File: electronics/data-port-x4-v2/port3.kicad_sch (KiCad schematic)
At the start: 30 parts, among them J301 PORT3, J302 PINS3, U301 TPS2553DBVR-1, U302 INA226AIDGSR, U303 USBLC6-2SC6, U305 H5VU25UC, U306 H5VU25UC, U307 LSF0108RKSR

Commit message: DATA x4 v2: datasheet audit fixes 1-9, conservative options, CFG_SEL 110
The DATA x4 v2 datasheet audit's fixes, approved by the user, plus the
conservative options that close U2, U8, U9 and U10:

- Core regulator (fixes 1-3).
  - L1 on a polarity-marked land: bench:L_Abracon_AOTA-B201610, RP's
    0.7 x 1.7 mm pads, the dot on pad 1 = +1V1 (U1's answer).
  - The block is Raspberry Pi's RP2350B Minimal R4-S1 one, turned 180
    degrees with U11, at their coordinates.  CIN and COUT sit on RP's
    0402 land (bench:C_0402_1005Metric_RP), so LX runs 0.3 mm between
    them.
  - Copper: their F.Cu areas (LX, +1V1 with the two V_OUT vias, PGND
    with its two vias, VIN) and their settings; VREG_FB taken at the
    V_OUT vias; CFILT on its own via.
  - The F.Cu GND pour leaves a hole round the block, so PGND meets the
    main GND only through its two vias.  No copper under LX and L1 on
    In1, In2 and B.Cu.
- Fix 4: C47 (DVDD pin 32) 100 nF -> 4.7 uF.
- Fix 5: R40 47k -> 10k, so GPIO45 stays >= -0.48 V; formula updated.
- Fix 6: UMW MAX809S (U5, C347371) drives the hub's RESET_N in place of
  R2/C6; C6 is its 100 nF.
- Fix 7: two H5VU25UC per port in flow-through.  VREF and RESET/BOOT
  sit at the header's two ends, so one part per end:
  - U108-U408 take VREF (logic only);
  - U109-U409 take RESET_N/BOOT_N with the 1k right behind them, fitted
    on the base too (schematic review N4).
  VREF and ports 1-3's RESET_N are drawn into their ESD pins; all 12
  lines checked in flow-through.
- Fixes 8, 9: the VREF isolation wording and the firmware rule (switches
  open below 0.65 V, in multi-dut-node.md); +5V_MX ~1-4 mA, FB1 and U3
  stale lines gone.
- Conservative options:
  - U2: R10 1M across XI-XO (C26083);
  - U8: R115-R415 100k in series with GPIO40-43;
  - U9: R11, R12 10k on the TCA6408A RESETs;
  - U10: C7, C8 4.7 uF.
- Hub on CFG_SEL 110, internal defaults with straps disabled (U11, U12
  answered by the user).  CFG_SEL1 and CFG_SEL2 pull up through their
  RN2/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
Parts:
- added R315: 100k, Resistor_SMD:R_0402_1005Metric, symbol Device:R
- added U308, U309: H5VU25UC, bench:DFN2510-10L_2.5x1.0mm_P0.5mm, symbol Power_Protection:TPD4E05U06DQA
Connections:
- net CP_VREF3: now also R315.1
- net GND: now also U308.3 (GND), U308.8 (GND), U309.3 (GND), U309.8 (GND)
- net PORT3_BOOT_N: now also U309.2 (D1-), U309.9 (NC)
- net PORT3_RST_N: now also U309.5 (D2-), U309.6 (NC)
- net PORT3_VREF: now also U308.5 (D2-), U308.6 (NC)
- new net CP_ADC3: R315.2
- no-connect marks 2 -> 12
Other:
- note added: "ESD on the header's VREF (U308, in flow-through: header → ESD → LSF0108 and divider) and on RESET_N / BOOT_N (U309: header → ESD → 1k)"

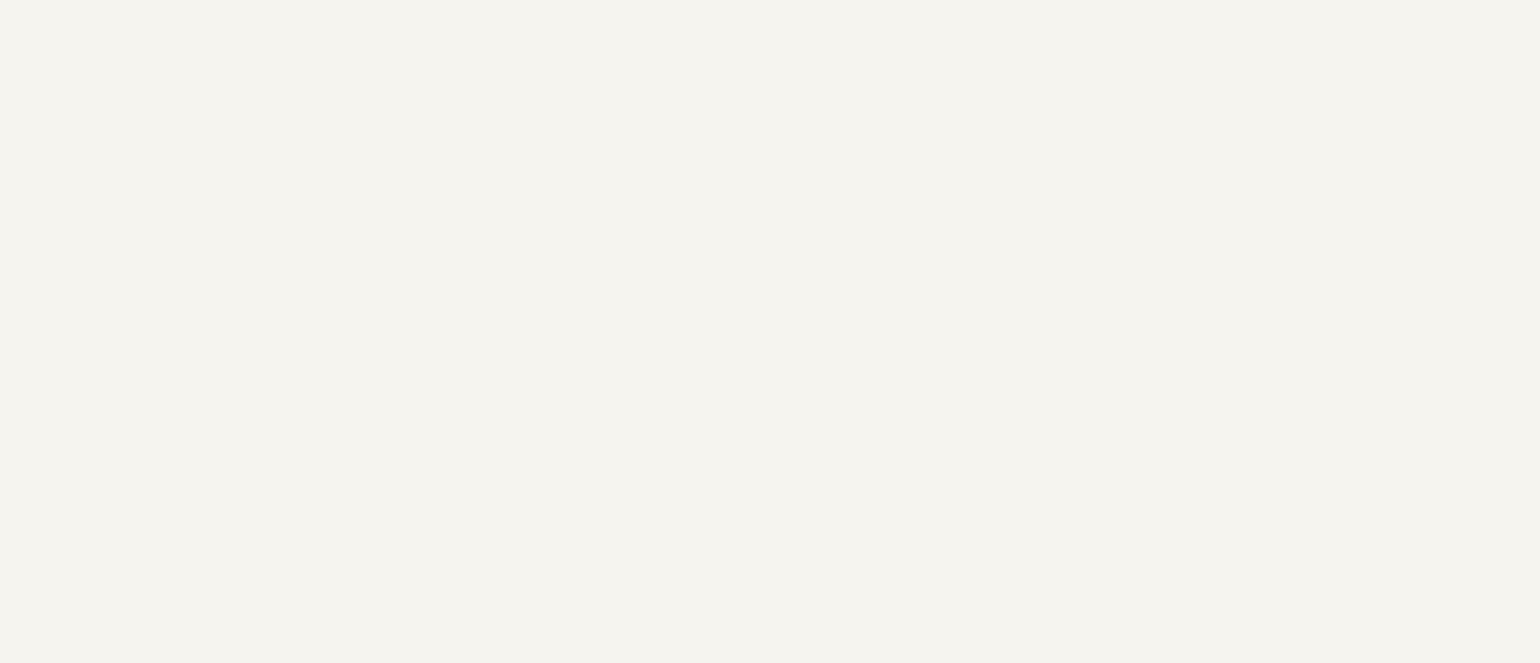
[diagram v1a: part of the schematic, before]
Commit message: DATA x4 v2: 32 labelled bring-up test points on the rear face
Eve's DFT rule on the DATA x4 v2.  Bare pads on B.Cu, mask open, no
paste, out of the BOM and the CPL (no part, no fee).  Each is named on
B.SilkS.  Supplies and GND are 1.5 mm, signals 1.0 mm (main's
"testpad1").  One table in design.py (TPS) holds every position, and
each sheet places its own.

- Co-processor row along the top edge: BOOT, RUN, SWDIO, SWCLK, GND,
  +3V3_CP.  SWD moves here from the front face.  +1V1 sits under the
  chip, on its own rear track.
- Matrix, left column: DAT, CK, STB2, GND, -5V, +5V_MX, GND; STB1 and
  MX RST on their own rear tracks.
- Supplies by the LDO: +3V3, GND, the lead's +5V.
- Hub: HUB RST, GND, 1V8.  Below J1: INT, SDA, SCL (the board side of
  the lead's isolation) and GND.
- Each port's FAULT_N (TP101-TP401) on its own rear track, and a GND by
  each pair's expander.
- Left out: VREF, RESET_N and BOOT_N (on the headers), the lead's lines
  (on J1) and the USB pairs.
- The logic's pads are marked LOGIC ONLY: the base leaves those parts
  off, so they float there.

Every pad is more than 2 mm from the THT pads and from J1, and clear of
the cradle ends, the push band and the notches.  The closest are TP23,
2.0 mm from J1's courtyard, and TP27, 2.1 mm from J101.

Routing: the old routing is seeded as protected wiring, so Freerouting
only adds the new links.  Where it gave up, the pad sits on a rear track
of its own net, or a short drawn link joins it (RUN onto CP_RUN's track,
+3V3_CP through a via to FB2).  The import's tidy pass is applied.

Checks: ERC 0, DRC 0 errors, unconnected 0, parity 0.  The 4
silk_over_copper warnings are the same on main.  Flow-through ESD check
BAD 0.  The fab outputs, panel, renders and GLBs are regenerated; the
BOM and CPL are unchanged.  docs/electronics.md lists the points, and
the "Test pads" table gains the board.

Co-Authored-By: Claude Opus 5.5 <noreply@anthropic.com>
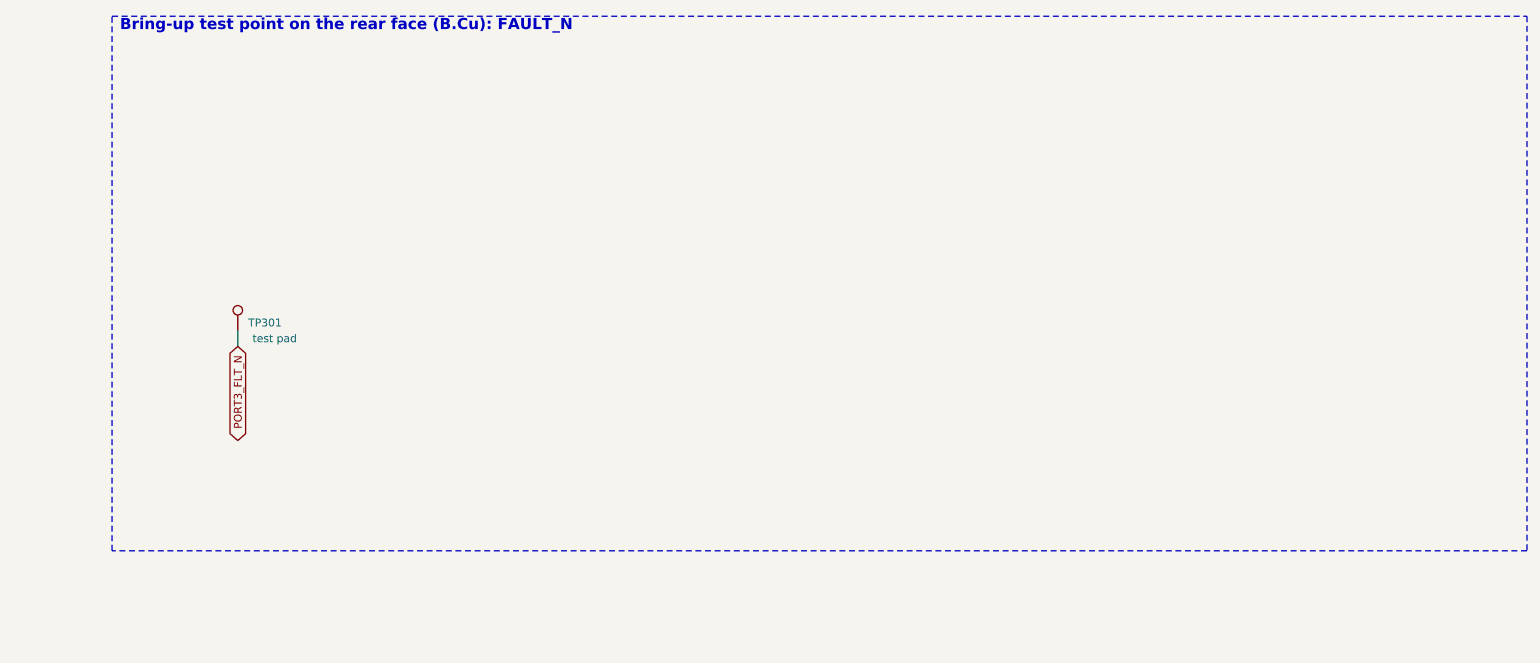
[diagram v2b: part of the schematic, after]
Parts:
- added TP301: test pad, TestPoint:TestPoint_Pad_D1.0mm, symbol Connector:TestPoint
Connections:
- net PORT3_FLT_N: now also TP301.1
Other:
- note added: "Bring-up test point on the rear face (B.Cu): FAULT_N"
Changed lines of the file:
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@@
 	)
 	(symbol
+		(lib_id "Connector:TestPoint")
+		(at 629.92 76.2 0)
+		(unit 1)
+		(exclude_from_sim no)
+		(in_bom no)
+		(on_board yes)
+		(dnp no)
+		(fields_autoplaced yes)
+		(property "Reference" "TP301"
+			(at 634.307 74.93 0)
+			(effects
+				(font
+					(size 1.27 1.27)
+				)
+			)
+		)
+		(property "Value" "test pad"
+			(at 635.882 77.47 0)
+			(effects
+				(font
+					(size 1.27 1.27)
+				)
+			)
+		)
+		(property "Footprint" "TestPoint:TestPoint_Pad_D1.0mm"
+			(at 629.92 76.2 0)
+			(effects
+				(font
+					(size 1.27 1.27)
+				)
+				(hide yes)
+			)
+		)
+		(property "Datasheet" ""
+			(at 629.92 76.2 0)
+			(effects
+				(font
+					(size 1.27 1.27)
+				)
+				(hide yes)
+			)
+		)
+		(property "Description" ""
+			(at 629.92 76.2 0)
+			(effects
+				(font
+					(size 1.27 1.27)
+				)
+				(hide yes)
+			)
+		)
+		(property "MPN" "test pad"
+			(at 629.92 76.2 0)
+			(effects
+				(font
+					(size 1.27 1.27)
+				)
+				(hide yes)
+			)
+		)
+		(property "Manufacturer" "-"
+			(at 629.92 76.2 0)
+			(effects
+				(font
+					(size 1.27 1.27)
+				)
+				(hide yes)
+			)
+		)
+		(pin "1"
+		)
+		(instances
+			(project "data-port-x4-v2"
+				(path "/6eede3c9-04e8-5df8-9dbf-dd766ca3200a/76303e69-a9f7-592c-9301-ccf39b66bdac"
+					(reference "TP301")
+					(unit 1)
+				)
+			)
+		)
+	)
+	(wire
+		(pts
+			(xy 629.92 76.2)
+			(xy 629.92 78.74)
+		)
+		(stroke
+			(width 0)
+			(type default)
+		)
+	)
+	(global_label "PORT3_FLT_N"
+		(shape bidirectional)
+		(at 629.92 78.74 270)
+		(fields_autoplaced yes)
+		(effects
+			(font
+				(size 1.27 1.27)
+			)
+			(justify right)
+		)
+		(property "Intersheetrefs" "${INTERSHEET_REFS}"
+			(at 629.92 78.74 0)
+			(effects
+				(font
+					(size 1.27 1.27)
+				)
+				(justify right)
+				(hide yes)
+			)
+		)
+	)
+	(symbol
 		(lib_id "Device:R_Shunt")
 		(at 116.84 58.42 0)
@@
 		(effects
 			(font
+				(size 1.8 1.8)
+				(bold yes)
+			)
+			(justify left bottom)
+		)
+	)
+	(rectangle
+		(start 609.6 25.4)
+		(end 838.2 111.76)
+		(stroke
+			(width 0.2)
+			(type dash)
+		)
+		(fill
+			(type none)
+		)
+	)
+	(text "Bring-up test point on the rear face (B.Cu): FAULT_N"
+		(exclude_from_sim no)
+		(at 610.87 27.94 0)
+		(effects
+			(font
